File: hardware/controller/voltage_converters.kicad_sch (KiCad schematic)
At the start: 16 parts, among them U3 EA8212HT6R, U4 EA8212HT6R

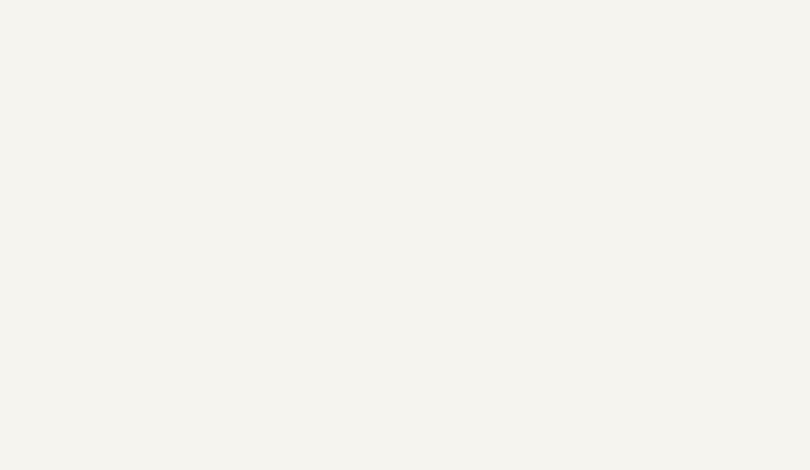
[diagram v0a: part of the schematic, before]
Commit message: adding labels and the barrel connector
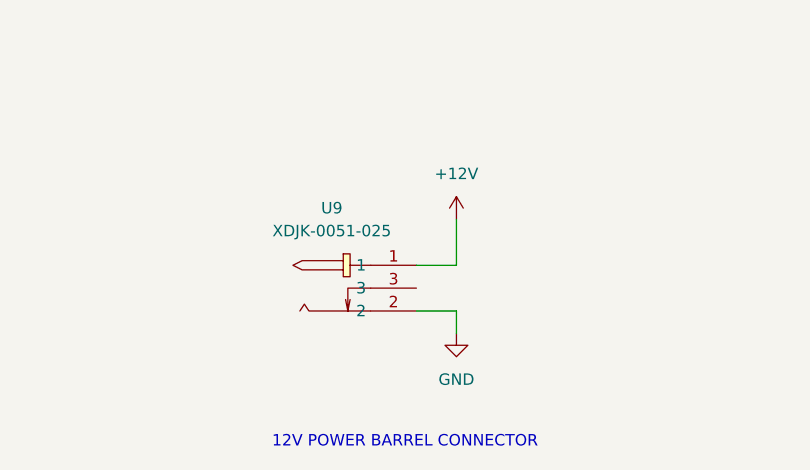
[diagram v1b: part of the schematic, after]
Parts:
- added U9: XDJK-0051-025, easyeda2kicad:DC-IN-TH_XDJK-0051-025, symbol easyeda2kicad:XDJK-0051-025
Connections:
- net +12V: now also U9.1
- net GND: now also U9.2
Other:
- note added: "12V POWER BARREL CONNECTOR"

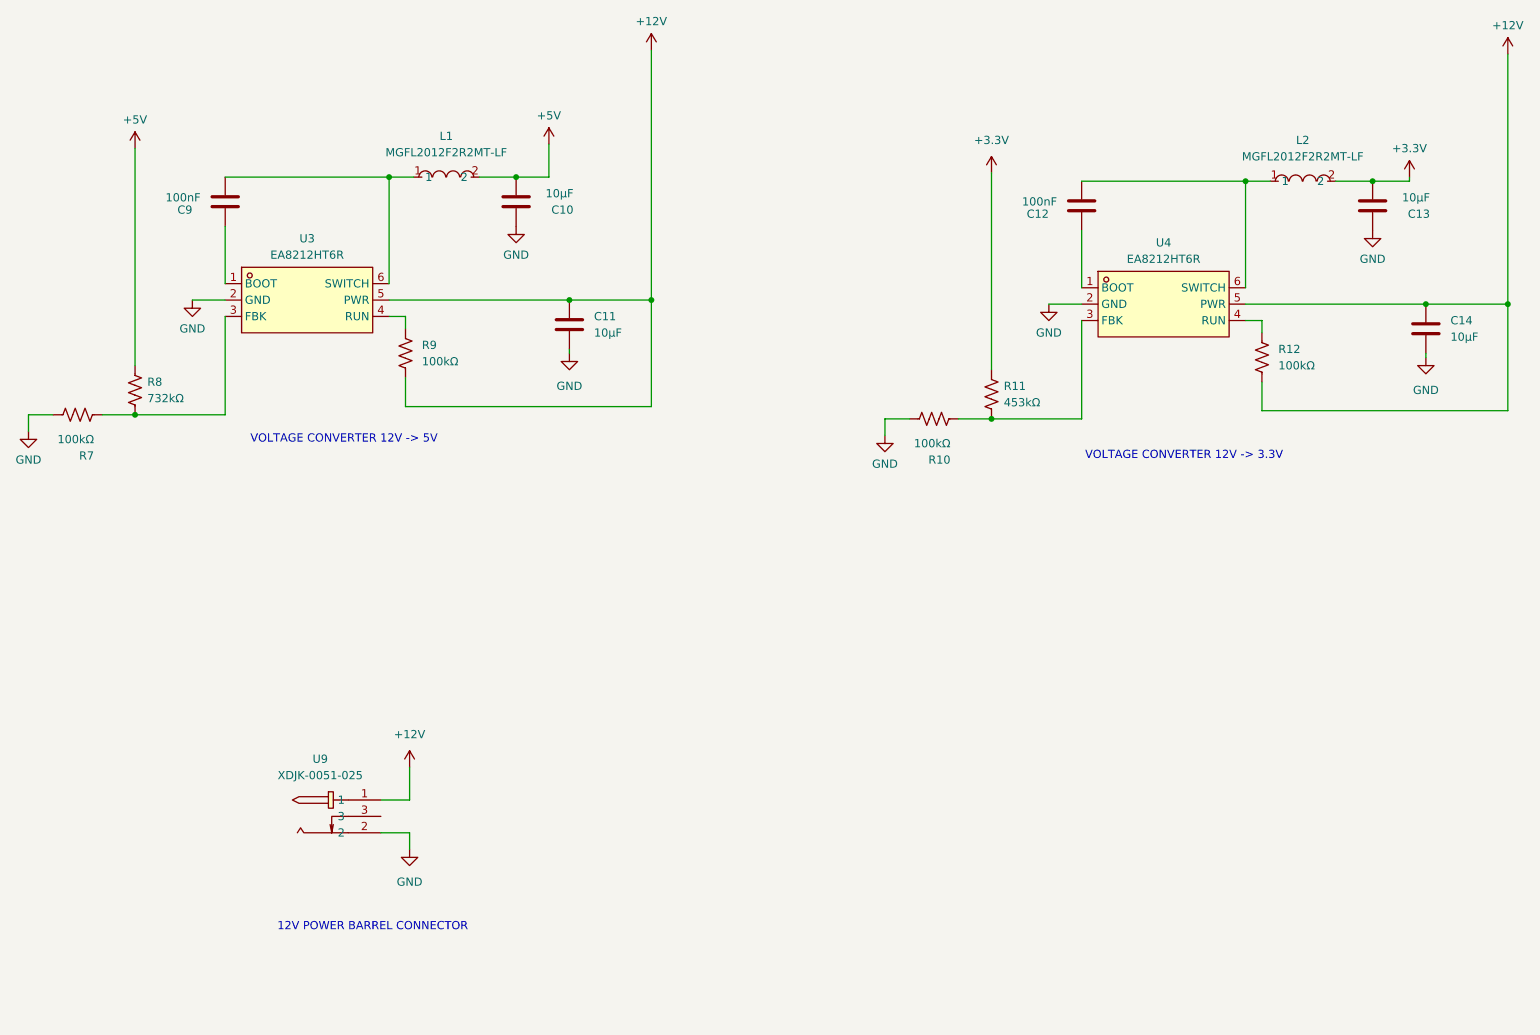
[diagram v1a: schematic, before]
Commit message: hook up all the dabao headers and one more voltage converter
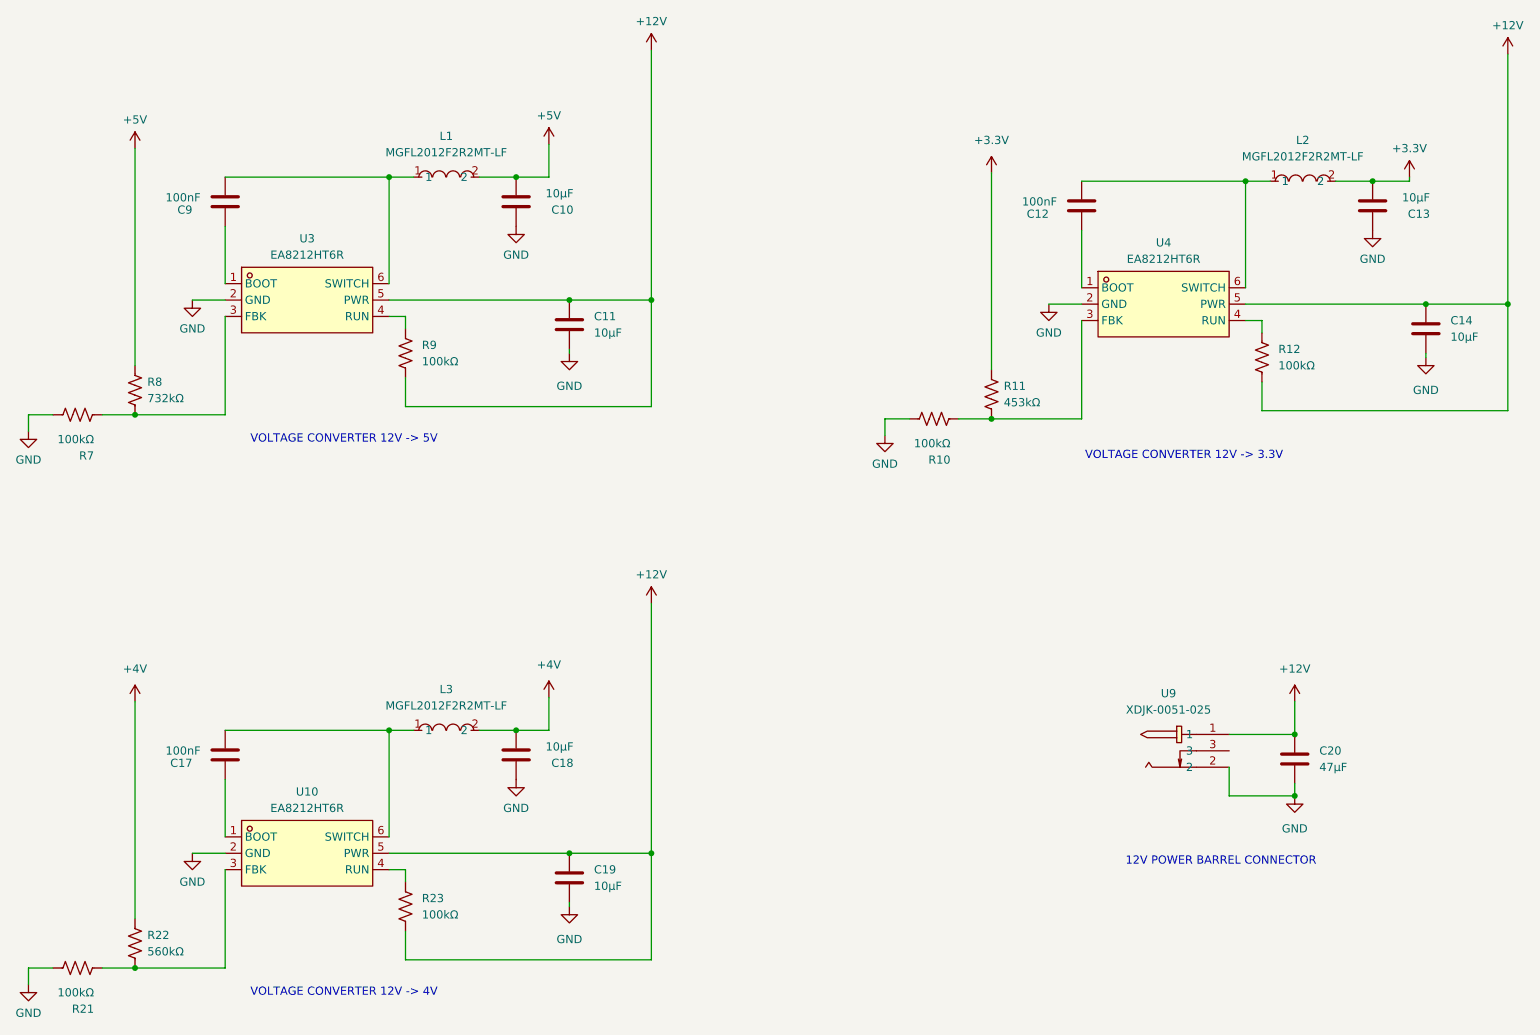
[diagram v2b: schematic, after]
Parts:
- added C17: 100nF, Capacitor_SMD:C_0402_1005Metric, symbol Device:C
- added C18, C19: 10µF, Capacitor_SMD:C_0603_1608Metric, symbol Device:C
- added C20: 47µF, Capacitor_SMD:C_1210_3225Metric, symbol Device:C
- added L3: MGFL2012F2R2MT-LF, footprints:L0805, symbol easyeda2kicad:MGFL2012F2R2MT-LF
- added R21, R23: 100kΩ, Resistor_SMD:R_0402_1005Metric, symbol Device:R_US
- added R22: 560kΩ, Resistor_SMD:R_0402_1005Metric, symbol Device:R_US
- added U10: EA8212HT6R, footprints:SOT-23-6_L2.9-W1.6-P0.95-LS2.8-BR, symbol new:EA8212HT6R
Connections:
- net +12V: now also C19.1, C20.2, R23.2, U10.5 (PWR)
- net GND: now also C18.2, C19.2, C20.1, R21.2, U10.2 (GND)
- new net: C17.1, U10.1 (BOOT)
- new net: C17.2, L3.1, U10.6 (SWITCH)
- new net: R21.1, R22.1, U10.3 (FBK)
- new net: R23.1, U10.4 (RUN)
- new net +4V: C18.1, L3.2, R22.2
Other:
- note added: "VOLTAGE CONVERTER 12V -> 4V"
- moved on the sheet: U9

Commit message: re-order the numbers on the schematic for tidiness
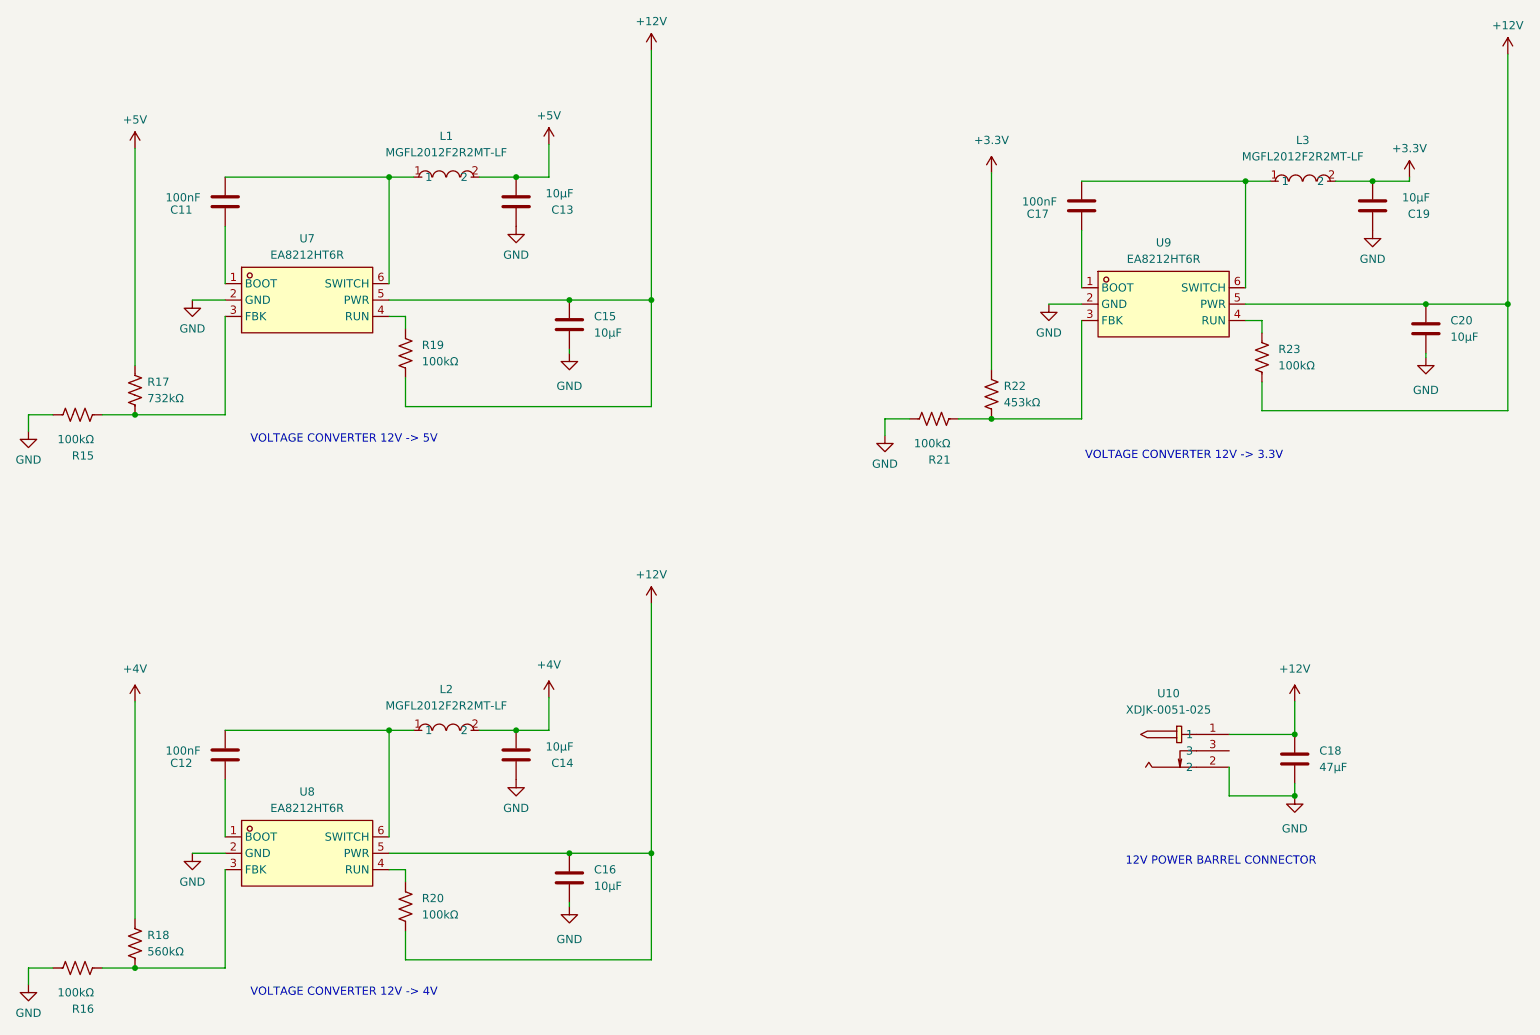
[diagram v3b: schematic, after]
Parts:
- renumbered C9 to C11, C17 to C12, C10 to C13, C18 to C14, C11 to C15, C19 to C16, C12 to C17, C20 to C18, C13 to C19, C14 to C20, L3 to L2, L2 to L3, R7 to R15, R21 to R16, R8 to R17, R22 to R18, R9 to R19, R23 to R20, R10 to R21, R11 to R22, R12 to R23, U9 to U10, U3 to U7, U10 to U8, U4 to U9

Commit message: renaming parts for consistency
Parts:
- C11, C12, C17: JLCPCB Part # C1525 -> (none); LCSC Part # (none) -> C1525
- C13, C14, C15, C16, C19, C20: JLCPCB Part # C96446 -> (none); LCSC Part # (none) -> C96446
- C18: JLCPCB Part # C77101 -> (none); LCSC Part # (none) -> C77101
- L1, L2, L3: JLCPCB # C281115 -> (none); LCSC Part # (none) -> C281115
- R15, R16, R19, R20, R21, R23: JLCPCB # C60491 -> (none); LCSC Part # (none) -> C60491
- R17: JLCPCB # C27016 -> (none); LCSC Part # (none) -> C27016
- R18: JLCPCB # C132339 -> (none); LCSC Part # (none) -> C132339
- R22: JLCPCB # C3013172 -> (none); LCSC Part # (none) -> C3013172
- U10: JLCPCB # C7498153 -> (none); LCSC Part # (none) -> C7498153
- U7, U8, U9: JLCPCB # C609568 -> (none); LCSC Part # (none) -> C609568
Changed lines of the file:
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@@
 			)
 		)
-		(property "JLCPCB Part #" "C77101"
+		(property "LCSC Part #" "C77101"
 			(at 221.615 133.35 0)
 			(hide yes)
@@
 			)
 		)
-		(property "JLCPCB #" "C281115"
+		(property "LCSC Part #" "C281115"
 			(at 90.17 60.96 0)
 			(hide yes)
@@
 			)
 		)
-		(property "JLCPCB #" "C7498153"
+		(property "LCSC Part #" "C7498153"
 			(at 205.105 152.4 0)
 			(hide yes)
@@
 			)
 		)
-		(property "JLCPCB Part #" "C96446"
+		(property "LCSC Part #" "C96446"
 			(at 109.22 66.04 90)
 			(hide yes)
@@
 			)
 		)
-		(property "JLCPCB Part #" "C96446"
+		(property "LCSC Part #" "C96446"
 			(at 109.22 151.765 90)
 			(hide yes)
@@
 			)
 		)
-		(property "JLCPCB #" "C281115"
+		(property "LCSC Part #" "C281115"
 			(at 222.885 61.595 0)
 			(hide yes)
@@
 			)
 		)
-		(property "LCSC Part Number" ""
-			(at 55.88 132.715 0)
-			(hide yes)
-			(show_name no)
-			(do_not_autoplace no)
-			(effects
-				(font
-					(size 1.27 1.27)
-				)
-			)
-		)
-		(property "JLCPCB Part #" "C1525"
+		(property "LCSC Part #" "C1525"
 			(at 55.88 132.715 0)
 			(hide yes)
@@
 			)
 		)
-		(property "JLCPCB #" "C3013172"
+		(property "LCSC Part #" "C3013172"
 			(at 174.625 76.835 0)
 			(hide yes)
@@
 			)
 		)
-		(property "JLCPCB #" "C132339"
+		(property "LCSC Part #" "C132339"
 			(at 41.91 161.925 0)
 			(hide yes)
@@
 			)
 		)
-		(property "JLCPCB #" "C60491"
+		(property "LCSC Part #" "C60491"
 			(at 83.82 70.485 0)
 			(hide yes)
@@
 			)
 		)
-		(property "LCSC Part Number" ""
-			(at 55.88 46.99 0)
-			(hide yes)
-			(show_name no)
-			(do_not_autoplace no)
-			(effects
-				(font
-					(size 1.27 1.27)
-				)
-			)
-		)
-		(property "JLCPCB Part #" "C1525"
+		(property "LCSC Part #" "C1525"
 			(at 55.88 46.99 0)
 			(hide yes)
@@
 			)
 		)
-		(property "JLCPCB #" "C60491"
+		(property "LCSC Part #" "C60491"
 			(at 165.735 80.645 0)
 			(hide yes)
@@
 			)
 		)
-		(property "JLCPCB #" "C609568"
+		(property "LCSC Part #" "C609568"
 			(at 68.58 168.275 0)
 			(hide yes)
@@
 			)
 		)
-		(property "JLCPCB #" "C60491"
+		(property "LCSC Part #" "C60491"
 			(at 33.02 165.735 0)
 			(hide yes)
@@
 			)
 		)
-		(property "JLCPCB Part #" "C96446"
+		(property "LCSC Part #" "C96446"
 			(at 100.965 46.99 90)
 			(hide yes)
@@
 			)
 		)
-		(property "JLCPCB #" "C281115"
+		(property "LCSC Part #" "C281115"
 			(at 90.17 146.685 0)
 			(hide yes)
@@
 			)
 		)
-		(property "JLCPCB #" "C609568"
+		(property "LCSC Part #" "C609568"
 			(at 201.295 83.185 0)
 			(hide yes)
@@
 			)
 		)
-		(property "JLCPCB #" "C609568"
+		(property "LCSC Part #" "C609568"
 			(at 68.58 82.55 0)
 			(hide yes)
@@
 			)
 		)
-		(property "JLCPCB #" "C60491"
+		(property "LCSC Part #" "C60491"
 			(at 216.535 71.12 0)
 			(hide yes)
@@
 			)
 		)
-		(property "JLCPCB #" "C60491"
+		(property "LCSC Part #" "C60491"
 			(at 33.02 80.01 0)
 			(hide yes)
@@
 			)
 		)
-		(property "JLCPCB Part #" "C96446"
+		(property "LCSC Part #" "C96446"
 			(at 100.965 132.715 90)
 			(hide yes)
@@
 			)
 		)
-		(property "JLCPCB #" "C27016"
+		(property "LCSC Part #" "C27016"
 			(at 41.91 76.2 0)
 			(hide yes)
@@
 			)
 		)
-		(property "JLCPCB #" "C60491"
+		(property "LCSC Part #" "C60491"
 			(at 83.82 156.21 0)
 			(hide yes)
@@
 			)
 		)
-		(property "JLCPCB Part #" "C96446"
+		(property "LCSC Part #" "C96446"
 			(at 233.68 47.625 90)
 			(hide yes)
@@
 			)
 		)
-		(property "JLCPCB Part #" "C96446"
+		(property "LCSC Part #" "C96446"
 			(at 241.935 66.675 90)
 			(hide yes)
@@
 			)
 		)
-		(property "LCSC Part Number" ""
-			(at 188.595 47.625 0)
-			(hide yes)
-			(show_name no)
-			(do_not_autoplace no)
-			(effects
-				(font
-					(size 1.27 1.27)
-				)
-			)
-		)
-		(property "JLCPCB Part #" "C1525"
+		(property "LCSC Part #" "C1525"
 			(at 188.595 47.625 0)
 			(hide yes)

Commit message: more footprint updating
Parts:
- L1, L2, L3: footprint footprints:L0805 -> easyeda2kicad:L0805
- U7, U8, U9: footprint footprints:SOT-23-6_L2.9-W1.6-P0.95-LS2.8-BR -> easyeda2kicad:SOT-23-6_L2.9-W1.6-P0.95-LS2.8-BR
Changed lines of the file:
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@@
 			)
 		)
-		(property "Footprint" "footprints:L0805"
+		(property "Footprint" "easyeda2kicad:L0805"
 			(at 90.17 50.8 0)
 			(hide yes)
@@
 			)
 		)
-		(property "Footprint" "footprints:L0805"
+		(property "Footprint" "easyeda2kicad:L0805"
 			(at 222.885 51.435 0)
 			(hide yes)
@@
 			)
 		)
-		(property "Footprint" "footprints:SOT-23-6_L2.9-W1.6-P0.95-LS2.8-BR"
+		(property "Footprint" "easyeda2kicad:SOT-23-6_L2.9-W1.6-P0.95-LS2.8-BR"
 			(at 68.58 158.115 0)
 			(hide yes)
@@
 			)
 		)
-		(property "Footprint" "footprints:L0805"
+		(property "Footprint" "easyeda2kicad:L0805"
 			(at 90.17 136.525 0)
 			(hide yes)
@@
 			)
 		)
-		(property "Footprint" "footprints:SOT-23-6_L2.9-W1.6-P0.95-LS2.8-BR"
+		(property "Footprint" "easyeda2kicad:SOT-23-6_L2.9-W1.6-P0.95-LS2.8-BR"
 			(at 201.295 73.025 0)
 			(hide yes)
@@
 			)
 		)
-		(property "Footprint" "footprints:SOT-23-6_L2.9-W1.6-P0.95-LS2.8-BR"
+		(property "Footprint" "easyeda2kicad:SOT-23-6_L2.9-W1.6-P0.95-LS2.8-BR"
 			(at 68.58 72.39 0)
 			(hide yes)
